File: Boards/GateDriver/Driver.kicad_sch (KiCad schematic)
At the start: 64 parts, among them U2 PUCC5880QDFCQ1

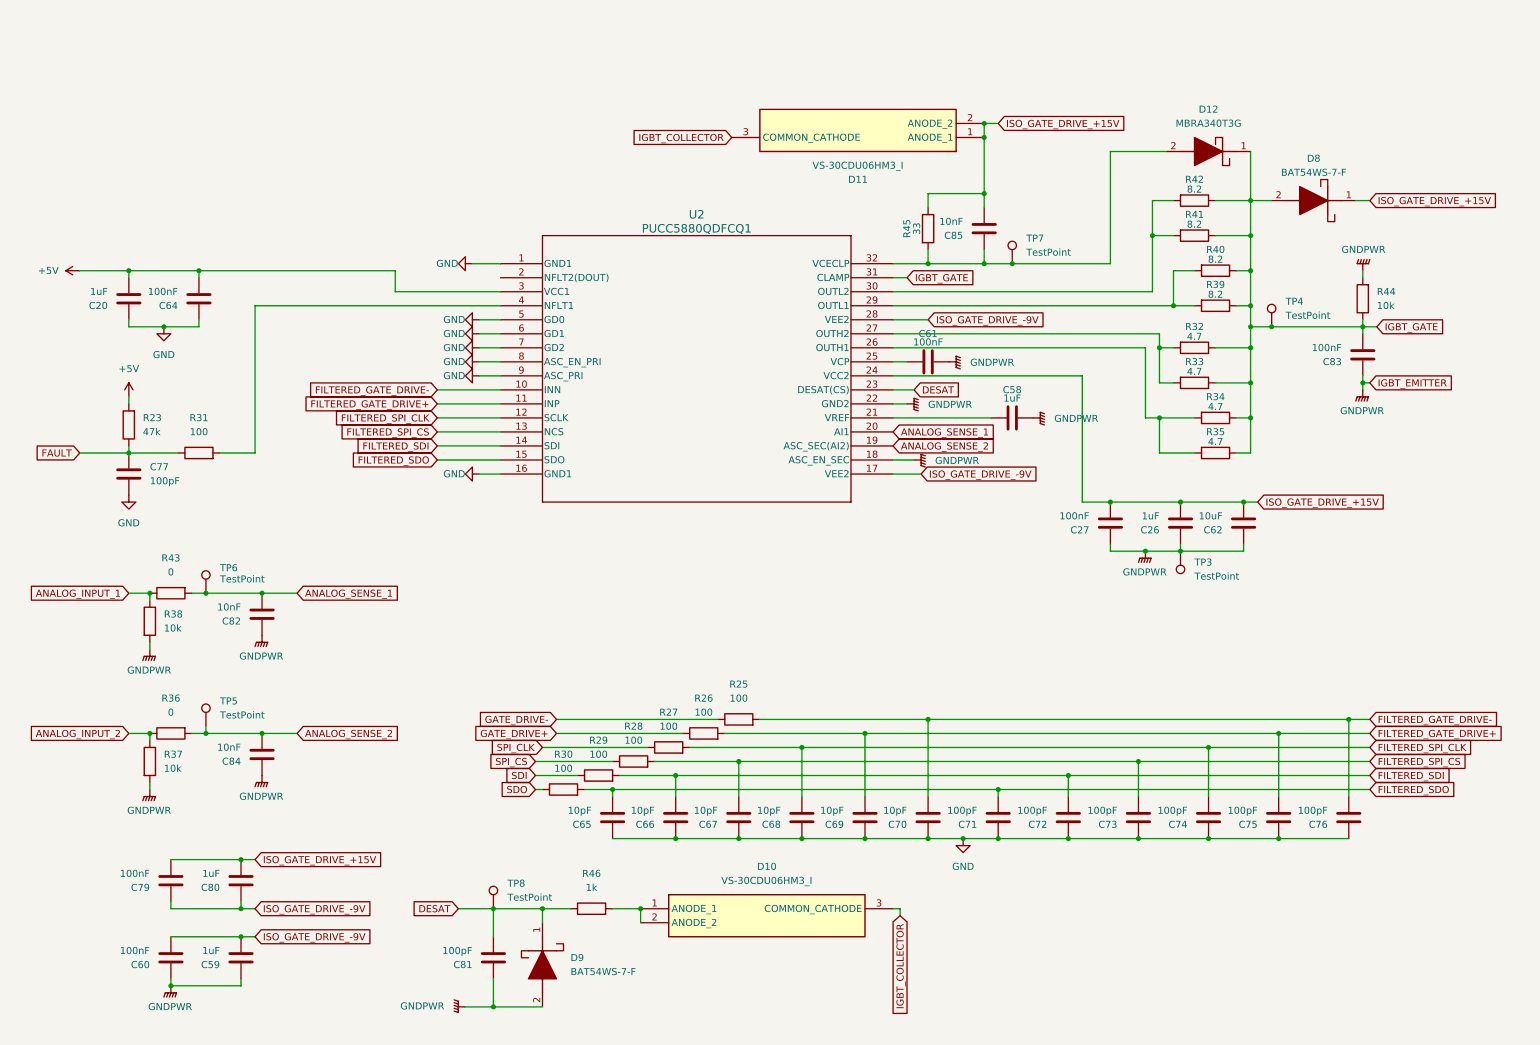
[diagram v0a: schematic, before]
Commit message: Update Gate Driver to use non NDA BS Chip
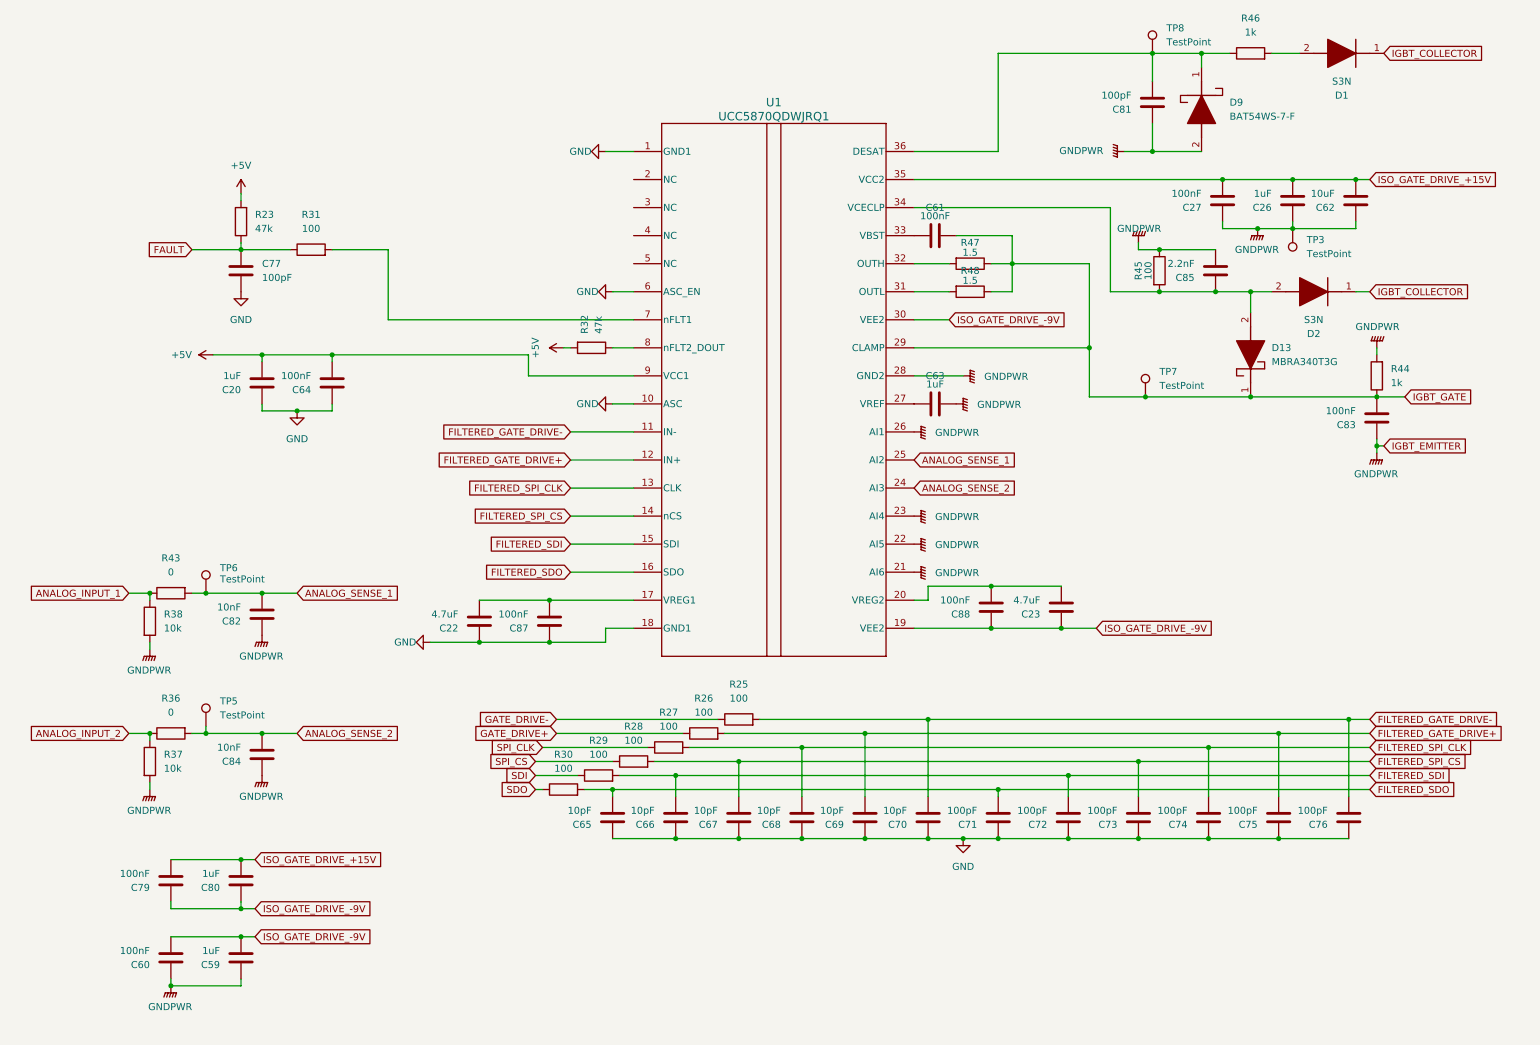
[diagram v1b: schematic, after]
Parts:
- removed C58: 1uF, Capacitor_SMD:C_1210_3225Metric_Pad1.33x2.70mm_HandSolder, symbol Device:C
- removed D10, D11: VS-30CDU06HM3_I, InverterCom:VS30CDU06HM3I, symbol InverterCom:VS-30CDU06HM3_I
- removed D12: MBRA340T3G, InverterCom:DIOM5226X220N, symbol InverterCom:MBRA340T3G
- removed D8: BAT54WS-7-F, InverterCom:SOD2513X120N, symbol InverterCom:BAT54WS-7-F
- removed R33, R34, R35: 4.7, Resistor_SMD:R_1210_3225Metric_Pad1.30x2.65mm_HandSolder, symbol Device:R
- removed R39, R40, R41, R42: 8.2, Resistor_SMD:R_1210_3225Metric_Pad1.30x2.65mm_HandSolder, symbol Device:R
- removed TP4: TestPoint, TestPoint:TestPoint_Loop_D2.54mm_Drill1.5mm_Beaded, symbol Connector:TestPoint
- removed U2: PUCC5880QDFCQ1, InverterCom:SSOP32_DFC_TEX-M, symbol InverterCom:PUCC5880QDFCQ1
- added C22, C23: 4.7uF, Capacitor_SMD:C_1210_3225Metric_Pad1.33x2.70mm_HandSolder, symbol Device:C
- added C63: 1uF, Capacitor_SMD:C_1210_3225Metric_Pad1.33x2.70mm_HandSolder, symbol Device:C
- added C87, C88: 100nF, Capacitor_SMD:C_1210_3225Metric_Pad1.33x2.70mm_HandSolder, symbol Device:C
- added D1, D2: S3N, InverterCom:DIOM8059X265N, symbol InverterCom:S3N
- added D13: MBRA340T3G, InverterCom:DIOM5226X220N, symbol InverterCom:MBRA340T3G
- added R47, R48: 1.5, Resistor_SMD:R_1210_3225Metric_Pad1.30x2.65mm_HandSolder, symbol Device:R
- added U1: UCC5870QDWJRQ1, InverterCom:DWJ0036A, symbol InverterCom:UCC5870QDWJRQ1
- C85: value 10nF -> 2.2nF
- R32: value 4.7 -> 47k
- R44: value 10k -> 1k
- R45: value 33 -> 100
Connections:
- net +5V: now also R32.2, U1.9 (VCC1)
- net ANALOG_SENSE_1: now also U1.25 (AI2)
- net ANALOG_SENSE_2: now also U1.24 (AI3)
- net FILTERED_GATE_DRIVE+: now also U1.12 (IN+)
- net FILTERED_GATE_DRIVE-: now also U1.11 (IN-)
- net FILTERED_SDI: now also U1.15 (SDI)
- net FILTERED_SDO: now also U1.16 (SDO)
- net FILTERED_SPI_CLK: now also U1.13 (CLK)
- net FILTERED_SPI_CS: now also U1.14 (nCS)
- net GND: now also C22.1, C87.1, U1.1 (GND1), U1.10 (ASC), U1.18 (GND1), U1.6 (ASC_EN)
- net GNDPWR: now also C85.2, R45.1, C63.1, U1.21 (AI6), U1.22 (AI5), U1.23 (AI4), U1.26 (AI1), U1.28 (GND2); no longer C61.1
- net IGBT_COLLECTOR: now also D1.1 (K), D2.1 (K)
- net IGBT_GATE: now also C61.1, TP7.1, D13.1 (K), R47.1, R48.1, U1.29 (CLAMP); no longer R32.1
- net ISO_GATE_DRIVE_+15V: now also U1.35 (VCC2); no longer C85.2, R45.1
- net ISO_GATE_DRIVE_-9V: now also C23.1, C88.1, U1.19 (VEE2), U1.30 (VEE2)
- net at C61.2: now also U1.33 (VBST)
- net at C85.1, R45.2: now also D13.2 (A), D2.2 (A), U1.34 (VCECLP); no longer TP7.1
- net at R46.2: now also D1.2 (A)
- net at R31.2: now also U1.7 (nFLT1)
- net DESAT: no longer names the net of C81.2, D9.1 (K), R46.1, TP8.1
- net DESAT: now also U1.36 (DESAT)
- new net: C63.2, U1.27 (VREF)
- new net: R47.2, U1.32 (OUTH)
- new net: R48.2, U1.31 (OUTL)
- new net: R32.1, U1.8 (nFLT2_DOUT)
- new net: C23.2, C88.2, U1.20 (VREG2)
- new net: C22.2, C87.2, U1.17 (VREG1)
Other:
- moved on the sheet: C20, C26, C27, C61, C62, C64, C77, C81, C83, C85, D9, R23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

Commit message: Update Layouts
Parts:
- R23, R32: value 47k -> 10k
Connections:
- net GND: now also U1.2 (NC), U1.3 (NC), U1.4 (NC), U1.5 (NC)
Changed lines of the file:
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@@
 	)
 	(junction
+		(at 125.73 41.91)
+		(diameter 0)
+		(color 0 0 0 0)
+	)
+	(junction
 		(at 217.17 161.29)
 		(diameter 0)
@@
 	)
 	(junction
+		(at 125.73 52.07)
+		(diameter 0)
+		(color 0 0 0 0)
+	)
+	(junction
 		(at 97.79 125.73)
 		(diameter 0)
@@
 	)
 	(junction
+		(at 125.73 46.99)
+		(diameter 0)
+		(color 0 0 0 0)
+	)
+	(junction
 		(at 156.21 161.29)
 		(diameter 0)
@@
 	)
 	(junction
+		(at 125.73 36.83)
+		(diameter 0)
+		(color 0 0 0 0)
+	)
+	(junction
 		(at 58.42 142.24)
 		(diameter 0)
@@
 	(wire
 		(pts
+			(xy 125.73 52.07) (xy 125.73 57.15)
+		)
+		(stroke
+			(width 0)
+			(type default)
+		)
+	)
+	(wire
+		(pts
 			(xy 179.07 115.57) (xy 190.5 115.57)
 		)
@@
 	(wire
 		(pts
+			(xy 237.49 81.28) (xy 260.35 81.28)
+		)
+		(stroke
+			(width 0)
+			(type default)
+		)
+	)
+	(wire
+		(pts
 			(xy 71.12 54.61) (xy 81.28 54.61)
 		)
@@
 	(wire
 		(pts
+			(xy 125.73 41.91) (xy 125.73 46.99)
+		)
+		(stroke
+			(width 0)
+			(type default)
+		)
+	)
+	(wire
+		(pts
 			(xy 256.54 49.53) (xy 256.54 50.8)
 		)
@@
 	(wire
 		(pts
+			(xy 125.73 46.99) (xy 125.73 52.07)
+		)
+		(stroke
+			(width 0)
+			(type default)
+		)
+	)
+	(wire
+		(pts
 			(xy 185.42 77.47) (xy 176.53 77.47)
 		)
@@
 	(wire
 		(pts
+			(xy 125.73 36.83) (xy 125.73 41.91)
+		)
+		(stroke
+			(width 0)
+			(type default)
+		)
+	)
+	(wire
+		(pts
 			(xy 41.91 187.96) (xy 41.91 186.69)
 		)
@@
 	(wire
 		(pts
-			(xy 237.49 81.28) (xy 260.35 81.28)
-		)
-		(stroke
-			(width 0)
-			(type default)
-		)
-	)
-	(wire
-		(pts
 			(xy 191.77 161.29) (xy 204.47 161.29)
 		)
@@
 			)
 		)
-		(property "Value" "47k"
+		(property "Value" "10k"
 			(at 119.3799 69.85 0)
 			(effects
@@
 			)
 		)
-		(property "Value" "47k"
+		(property "Value" "10k"
 			(at 57.15 50.7999 0)
 			(effects
